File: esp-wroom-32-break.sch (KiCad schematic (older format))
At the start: 22 parts, among them CON1 Micro_SD_Card, IC1 FT232RQ, P1 CONN_01X17, P2 CONN_01X17, P3 USB_OTG, Q1 MMBT3904, Q2 MMBT3904, SW1 SWITCH_DPST, U1 ESP32-WROOM, U2 NJU7223DL1-33

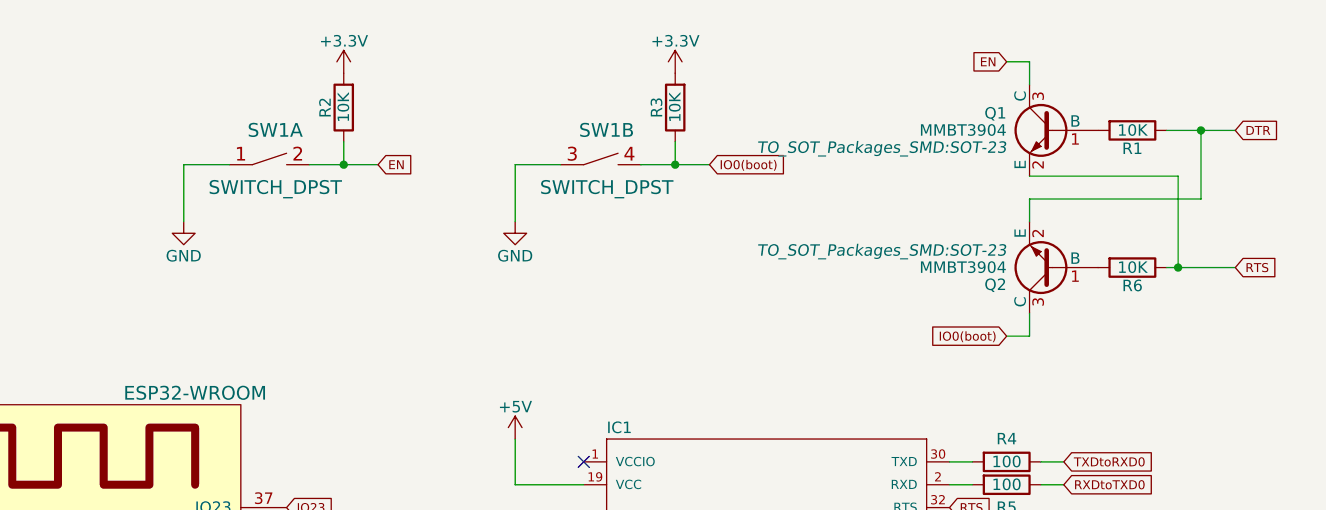
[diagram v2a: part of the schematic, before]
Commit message: Put footprints for rev1.1
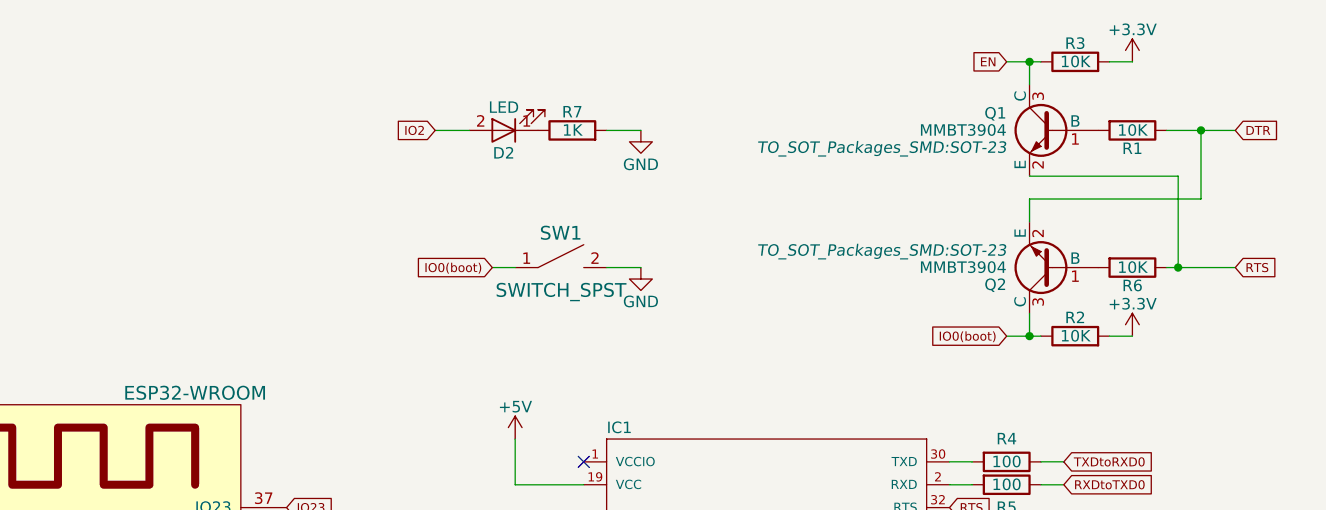
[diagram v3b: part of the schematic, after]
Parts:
- removed SW1: SWITCH_DPST, symbol SWITCH_DPST
- added D2: LED, LEDs:LED_0603, symbol LED
- added R7: 1K, Resistors_SMD:R_0603, symbol R
- added SW1: SWITCH_SPST, switch:SKRPACE010, symbol SWITCH_SPST
- P1, P2: footprint Pin_Headers:Pin_Header_Straight_1x17_Pitch2.00mm -> Pin_Headers:Pin_Header_Straight_1x17_Pitch2.54mm
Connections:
- net EN: now also R3.1; no longer R2.1
- net GND: now also R7.2, SW1.2
- net IO0(boot): now also R2.1, SW1.1; no longer R3.1
- net IO2: now also D2.2 (A)
- new net: D2.1 (K), R7.1
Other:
- moved on the sheet: R2, R3

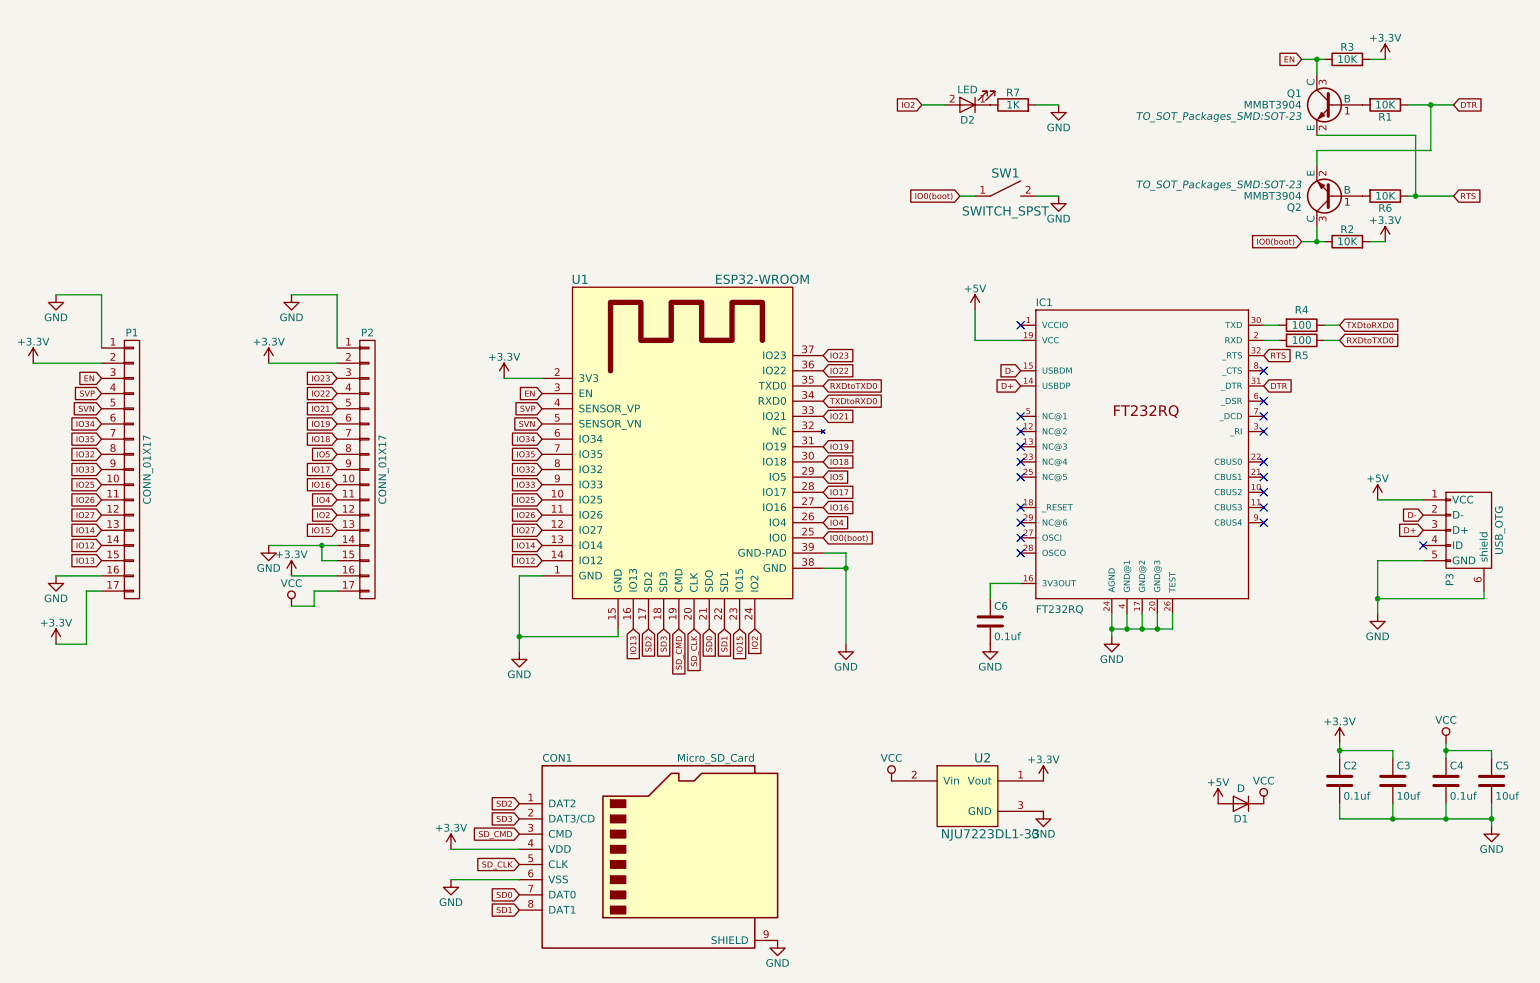
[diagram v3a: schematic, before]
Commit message: Add registers to pull up SD signals and reset button etc
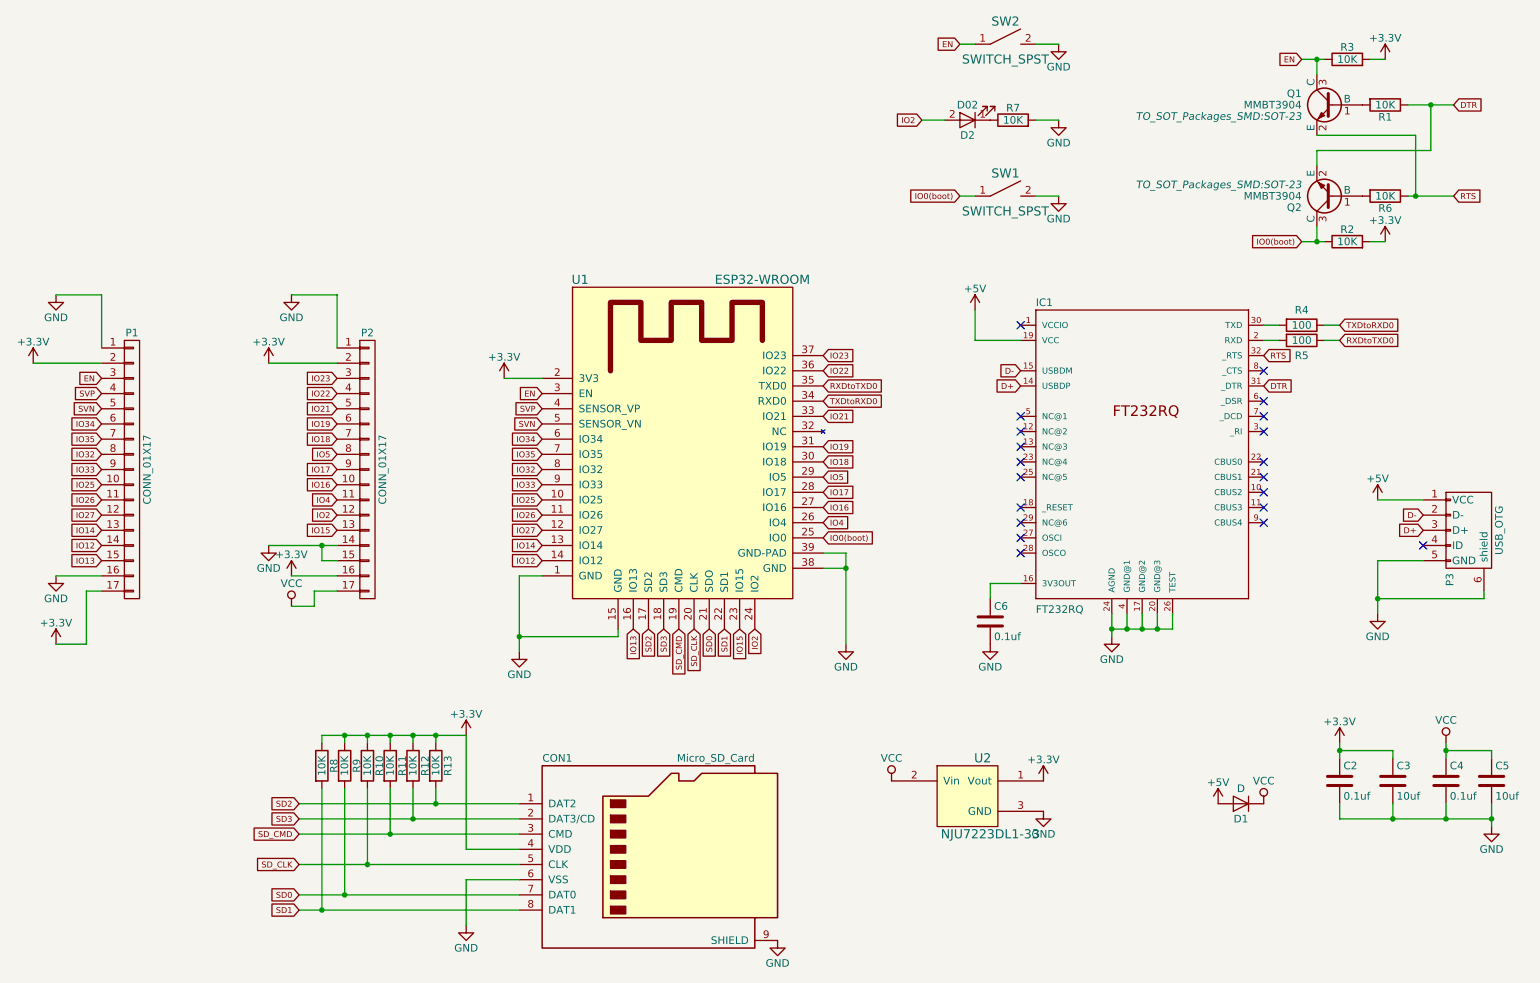
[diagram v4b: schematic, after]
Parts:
- added R10, R11, R12, R13, R8, R9: 10K, Resistors_SMD:R_0603, symbol R
- added SW2: SWITCH_SPST, switch:SKRPACE010, symbol SWITCH_SPST
- D2: value LED -> D02
- IC1: footprint ftdi232rq:ft232rq -> ftdi232rq:FR232RQ
- R7: value 1K -> 10K
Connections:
- net +3V3: now also R10.1, R11.1, R12.1, R13.1, R8.1, R9.1
- net EN: now also SW2.1
- net GND: now also SW2.2
- net SD0: now also R9.2
- net SD1: now also R8.2
- net SD2: now also R13.2
- net SD3: now also R12.2
- net SD_CLK: now also R10.2
- net SD_CMD: now also R11.2
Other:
- moved on the sheet: D2, R7
